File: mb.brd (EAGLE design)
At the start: 70 x 85 mm, 33 parts, among them J1 PJ-002BH-SMT-TR, J2 MOLEX_70543-0003MOLEX_70543-0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, J3 MOLEX_70543-0003MOLEX_70543-0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, J4 MOLEX_70543-0003MOLEX_70543-0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, J5 MOLEX_70543-0003MOLEX_70543-0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, Q1 TN0702N3-G, Q2 TN0702N3-G, Q3 TN0702N3-G, Q4 TN0702N3-G, U1 PEM1-S12-S5-S

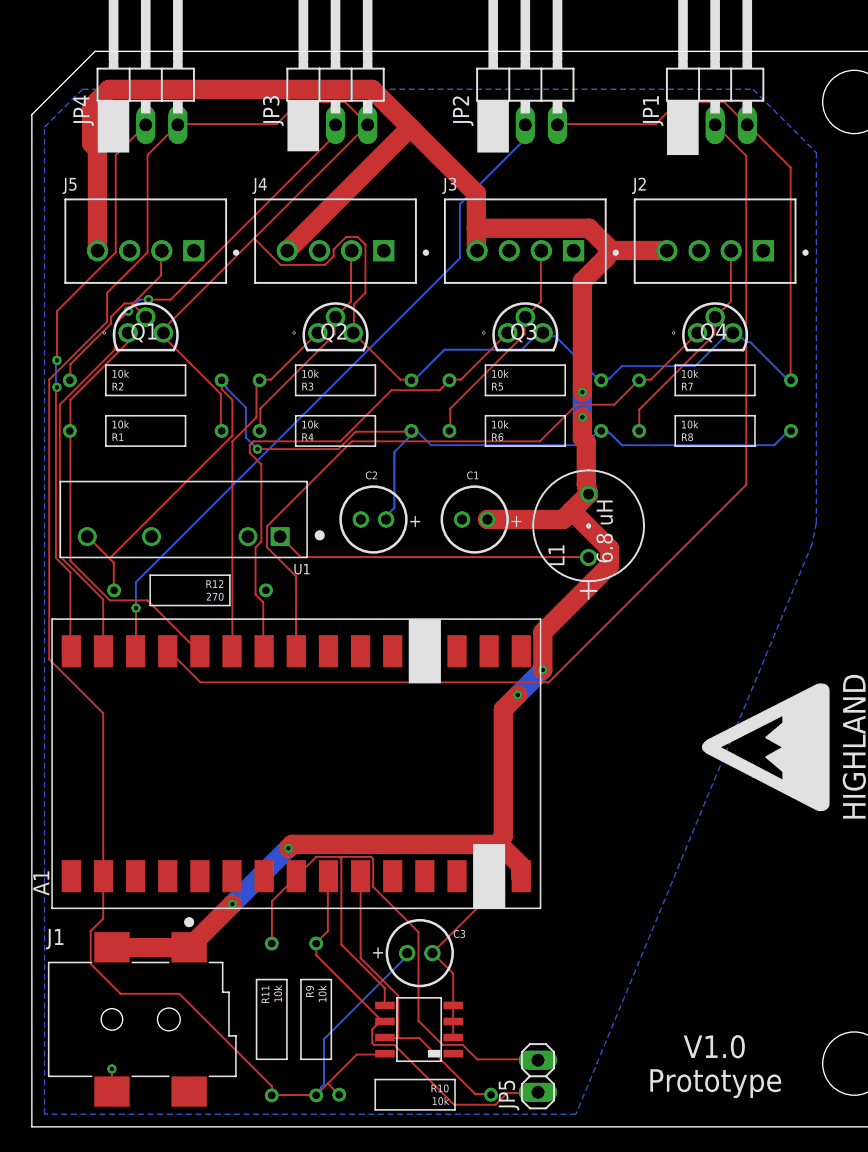
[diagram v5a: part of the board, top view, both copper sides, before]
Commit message: REV2
Correcting mosfet pinout
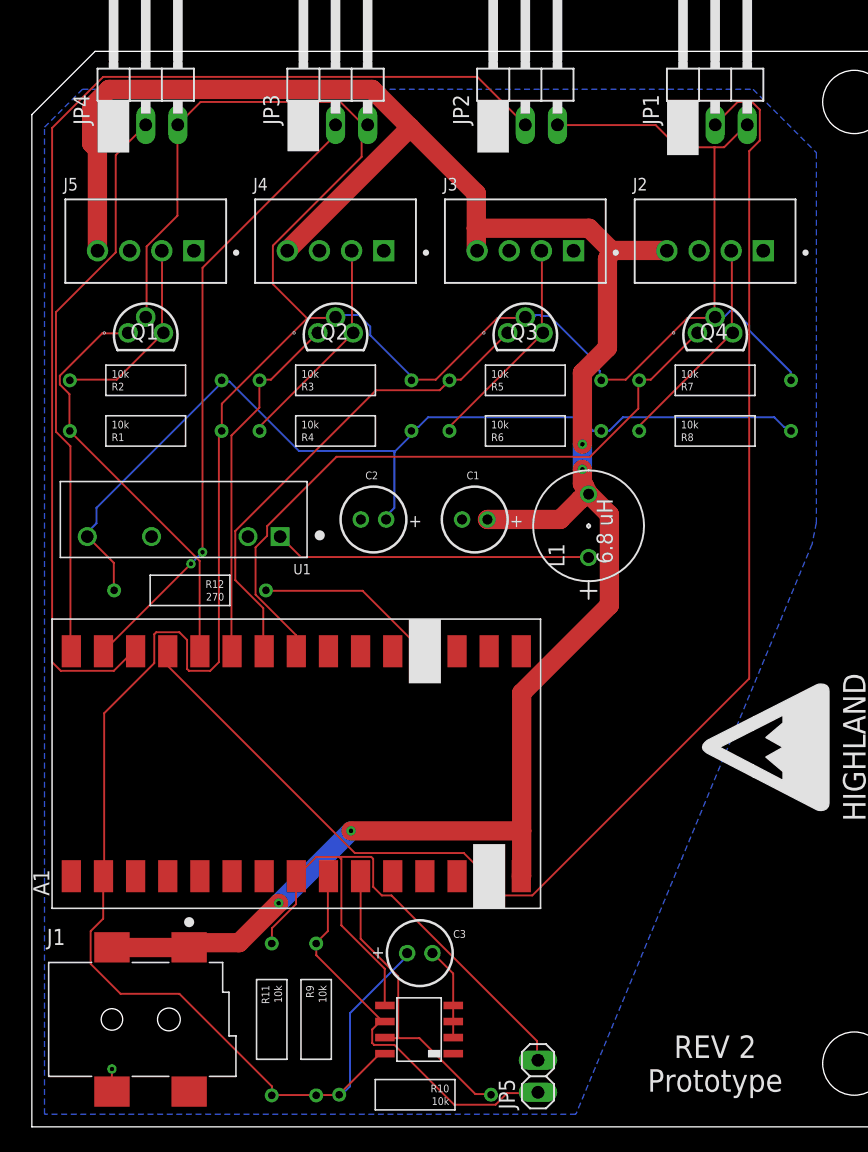
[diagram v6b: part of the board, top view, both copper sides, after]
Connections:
- net +3.3V: now also Q1.2, Q2.2, Q3.2, Q4.2; no longer Q1.3, Q2.3, Q3.3, Q4.3
- net LED1: now also Q4.3; no longer Q4.2
- net LED2: now also Q3.3; no longer Q3.2
- net LED3: now also Q2.3; no longer Q2.2
- net LED4: now also Q1.3; no longer Q1.2
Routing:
- net BOOL2: track 54.4 -> 90.4 mm, vias 1 -> 0
- net BOOL1: track 82.7 -> 112.9 mm
- net +3.3V: track 266.0 -> 242.9 mm
- net GND: track 18.9 -> 25.6 mm
- net +5V: track 82.7 -> 77.7 mm, vias 1 -> 0
- net BOOL3: track 53.5 -> 49.2 mm
- net SDA: track 51.1 -> 47.9 mm
- net LC2: track 41.2 -> 38.5 mm
- net LC1: track 51.2 -> 53.2 mm
- net +12V: track 177.6 -> 179.1 mm, vias 6 -> 4
- net BOOL4: track 45.1 -> 45.0 mm, vias 2 -> 0
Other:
- board text added: "REV 2 Prototype"
- board text removed: "V1.0 Prototype"

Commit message: Fixing D0 B0 flip
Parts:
- renumbered J2 to LED1, J3 to LED2, J4 to LED3, J5 to LED4
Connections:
- net GND: now also LED1.2, LED2.2, LED3.2, LED4.2; no longer LED1.3, LED2.3, LED3.3, LED4.3
- net LED1: now also LED1.3; no longer LED1.2
- net LED2: now also LED2.3; no longer LED2.2
- net LED3: now also LED3.3; no longer LED3.2
- net LED4: now also LED4.3; no longer LED4.2
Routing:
- net LED1: track 17.4 -> 23.5 mm
- net LED3: track 17.5 -> 18.6 mm
- net LED2: track 17.5 -> 18.6 mm
- net LED4: track 15.6 -> 16.7 mm
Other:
- board text added: "SCL"
- board text added: "SDA"
